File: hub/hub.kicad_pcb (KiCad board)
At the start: 2 copper layers, 18 parts, among them J1 C10418, U1 FE1.1s

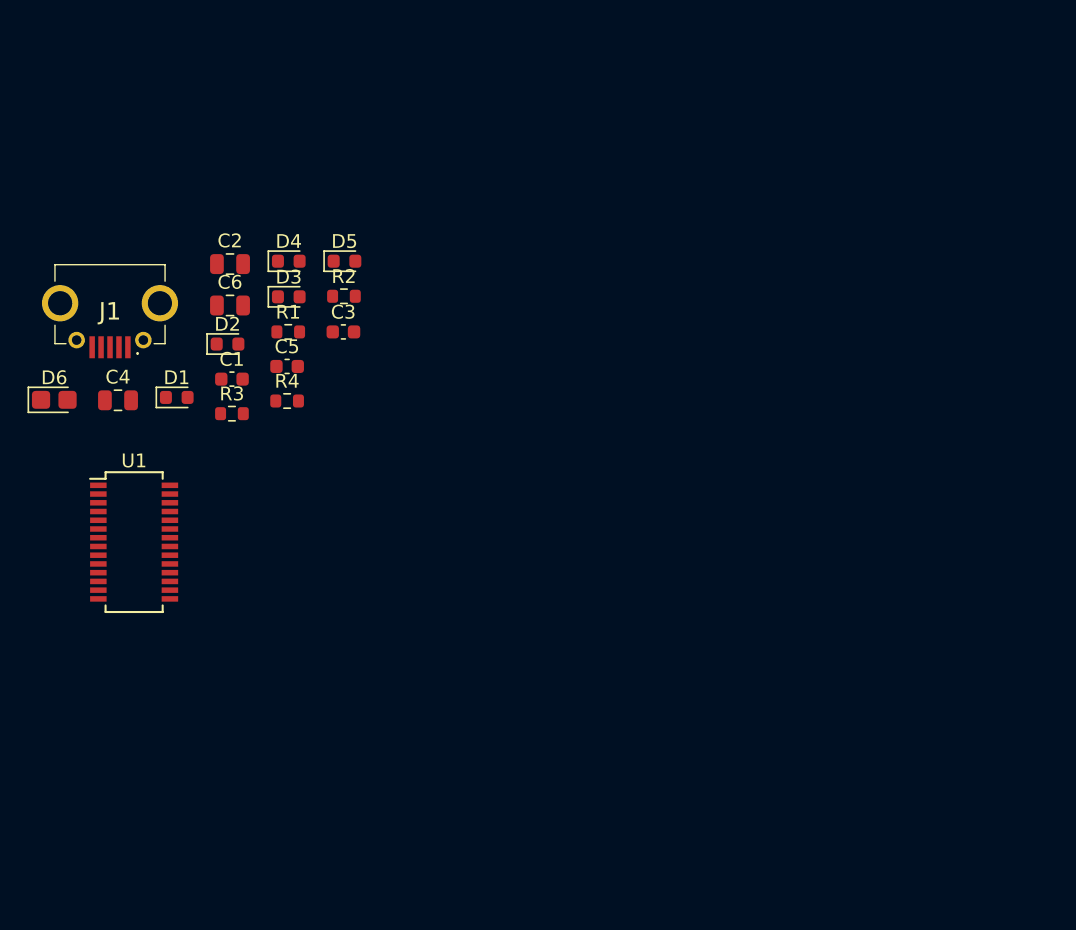
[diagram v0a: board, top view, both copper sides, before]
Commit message: V3.4 finished and ordered
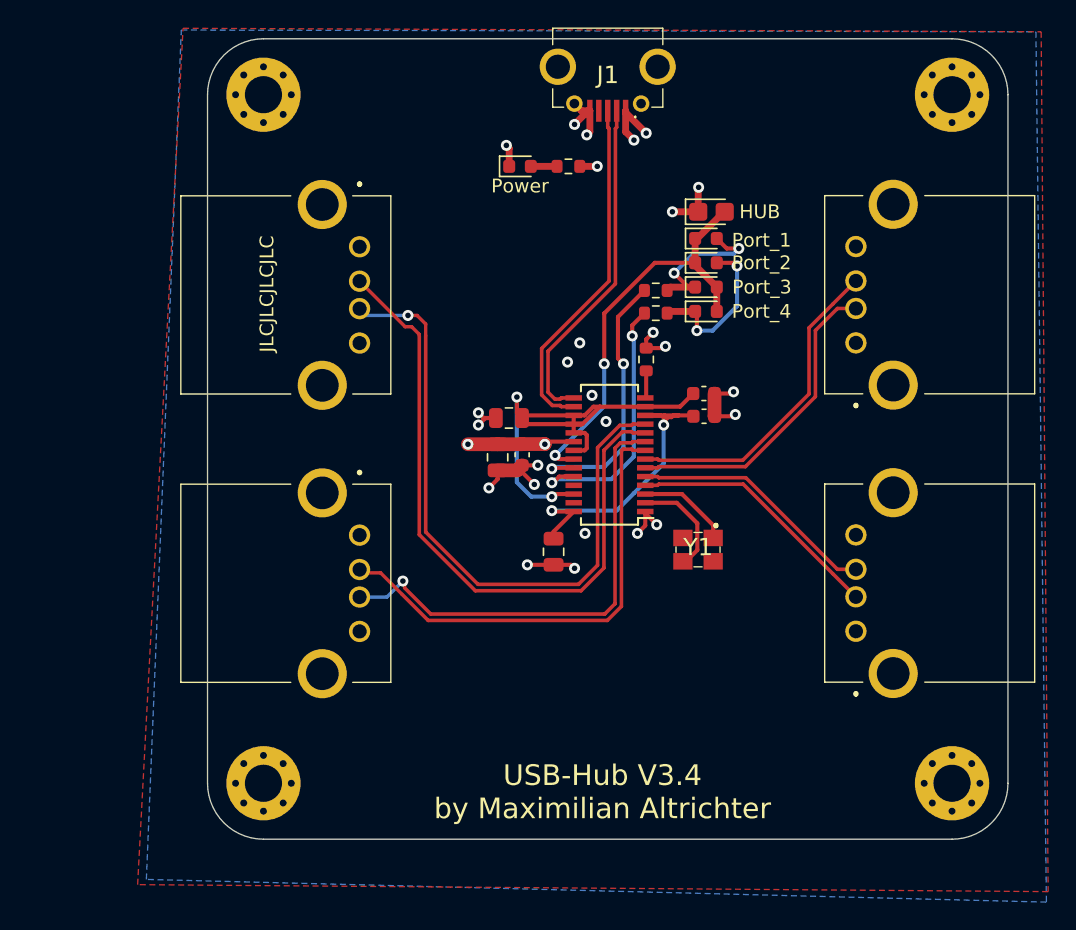
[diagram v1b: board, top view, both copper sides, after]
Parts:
- added H1: MountingHole_Pad, MountingHole:MountingHole_2.7mm_M2.5_Pad_Via, F.Cu at (189.4, 104.8)
- added H2: MountingHole_Pad, MountingHole:MountingHole_2.7mm_M2.5_Pad_Via, F.Cu at (139.3, 104.8)
- added H3: MountingHole_Pad, MountingHole:MountingHole_2.7mm_M2.5_Pad_Via, F.Cu at (139.3, 54.7)
- added H4: MountingHole_Pad, MountingHole:MountingHole_2.7mm_M2.5_Pad_Via, F.Cu at (189.4, 54.7)
- added J2: USB_A, SamacSys_Parts:676430910, F.Cu at (146.3, 65.8)
- added J3: USB_A, SamacSys_Parts:676430910, F.Cu at (146.3, 86.7)
- added J4: USB_A, SamacSys_Parts:676430910, F.Cu at (182.4, 93.7)
- added J5: USB_A, SamacSys_Parts:676430910, F.Cu at (182.4, 72.8)
- added Y1: 12 MHZ, crystal_12MHz:X322512MSB4SI, F.Cu at (170.9, 87.8)
- D6: value HUB_STATUS -> HUB
- moved D6 49.7 mm to (171.9, 63.2)
- moved J1 40.0 mm to (164.3, 52.9)
- moved D2 35.6 mm to (171.5, 65.2)
- moved U1 35.1 mm to (164.5, 80.9), turned to 180 degrees
- moved R3 32.1 mm to (167.8, 69.0)
- moved C5 30.5 mm to (171.3, 78.1)
- moved D3 30.3 mm to (171.5, 68.7)
- moved D4 30.3 mm to (171.5, 67.0)
- moved D1 30.1 mm to (158.0, 59.9)
- moved C6 29.5 mm to (160.4, 88.0), turned to 270 degrees
- moved C4 28.4 mm to (157.2, 78.2), turned to 180 degrees
- moved R4 27.5 mm to (167.8, 70.6)
- moved C3 26.6 mm to (171.3, 76.5)
- moved D5 26.5 mm to (171.5, 70.5)
- moved C2 24.0 mm to (156.3, 81.1), turned to 270 degrees
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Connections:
- U1 pad 2: Net-(U1-Pad2) -> /XOUT
- U1 pad 3: Net-(U1-Pad3) -> /XIN
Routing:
- net /D1_N: track 0.00 -> 48.4 mm
- net /D1_P: track 0.00 -> 47.7 mm, vias 0 -> 1
- net +3V3: track 0.00 -> 36.3 mm, vias 0 -> 2
- net /D2_P: track 0.00 -> 34.3 mm, vias 0 -> 1
- net /D2_N: track 0.00 -> 34.1 mm
- net GND: track 0.00 -> 33.4 mm, vias 0 -> 23
- net /DRV: track 0.00 -> 30.3 mm, vias 0 -> 2
- net /D_P: track 0.00 -> 25.4 mm
- net /D_N: track 0.00 -> 24.6 mm
- net /D3_P: track 0.00 -> 23.6 mm
- net +1V8: track 0.00 -> 23.5 mm, vias 0 -> 2
- net /D3_N: track 0.00 -> 22.9 mm
- net /LED_2: track 0.00 -> 20.0 mm, vias 0 -> 2
- net /LED_1: track 0.00 -> 19.8 mm, vias 0 -> 2
- net /D4_N: track 0.00 -> 18.7 mm
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- added copper zone on In2.Cu, net +5V
- added copper zone on B.Cu, net GND
- added copper zone on F.Cu, net GND
- added copper zone on In1.Cu, net GND
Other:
- board outline added: 58.2 x 58.2 mm
- copper layers 2 -> 4
- board text added: "JLCJLCJLCJLC"
- board text added: "USB-Hub V3.4 by Maximilian Altrichter"
